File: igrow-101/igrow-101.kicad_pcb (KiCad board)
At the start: 2 copper layers, 49.8 x 39.5 mm, 30 parts, among them P1 CONN_02X05, Q1 NPN, Q2 NPN, Q3 NPN, SW1 SW_PUSH, U1 NRF51822-MODULE, U2 SHT21, U3 TL972

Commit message: Rework with 0.508mm/20mil minimum track widths
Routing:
- net GND: track 0.00 -> 115.4 mm
- net VCC: track 0.00 -> 88.7 mm, vias 0 -> 1
- net Net-(Q1-Pad2): track 0.00 -> 24.5 mm
- net Net-(Q2-Pad2): track 0.00 -> 17.6 mm
- net Net-(R10-Pad2): track 0.00 -> 13.8 mm
- net Net-(R3-Pad2): track 0.00 -> 13.2 mm
- net Net-(Q3-Pad2): track 0.00 -> 12.0 mm
- net Net-(R2-Pad2): track 0.00 -> 11.4 mm
- net Net-(D4-Pad1): track 0.00 -> 10.5 mm
- net Net-(R1-Pad2): track 0.00 -> 9.58 mm
- net Net-(D4-Pad2): track 0.00 -> 8.86 mm
- net Net-(P1-Pad4): track 0.00 -> 7.10 mm
- net Net-(D3-Pad2): track 0.00 -> 6.00 mm
- net Net-(U1-Pad36): track 0.00 -> 5.73 mm
- net Net-(U1-Pad35): track 0.00 -> 5.70 mm
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- added copper zone on F.Cu, net GND

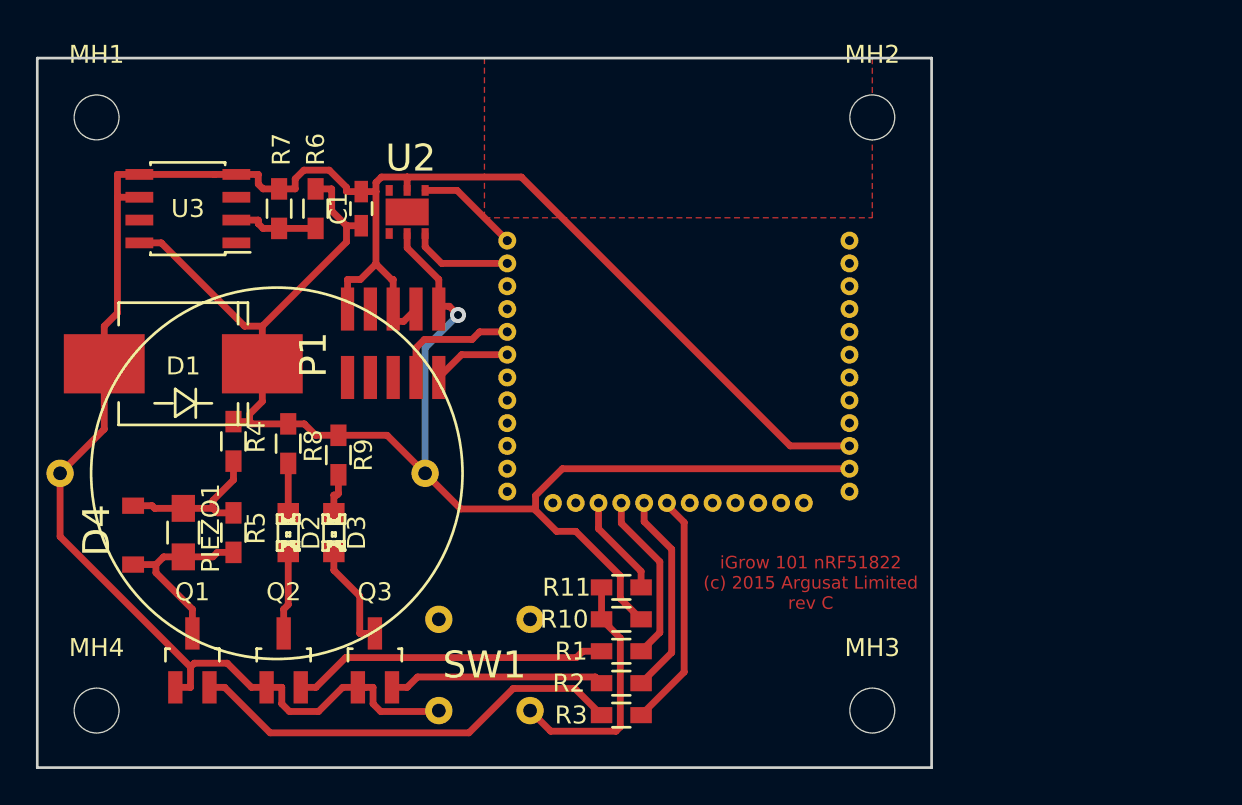
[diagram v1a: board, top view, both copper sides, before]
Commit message: First pass at board revision D - use direct connected IR LEDs for sensing
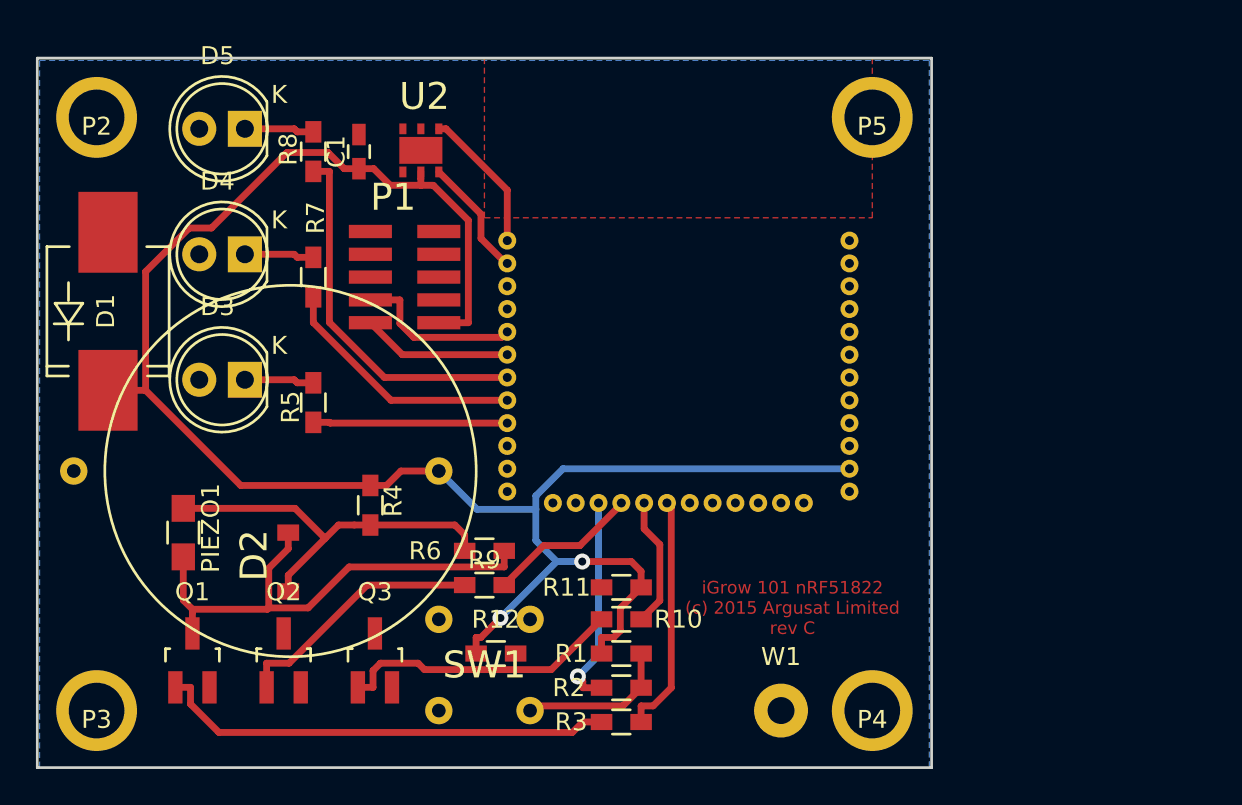
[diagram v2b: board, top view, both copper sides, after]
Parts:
- removed MH1, MH2, MH3, MH4: MountingHole_2-5mm, Mounting_Holes:MountingHole_2-5mm
- removed U3: TL972, Housings_SOIC:SOIC-8_3.9x4.9mm_Pitch1.27mm
- added D5: LED, LEDs:LED-5MM, F.Cu at (142.9, 97.2)
- added P2: CONN_01X01, igrow:MountingHole_M3, F.Cu at (134.6, 96.5)
- added P3: CONN_01X01, igrow:MountingHole_M3, F.Cu at (134.6, 129.5)
- added P4: CONN_01X01, igrow:MountingHole_M3, F.Cu at (177.8, 129.5)
- added P5: CONN_01X01, igrow:MountingHole_M3, F.Cu at (177.8, 96.5)
- added R12: R, Resistors_SMD:R_0603_HandSoldering, F.Cu at (156.8, 126.4)
- added W1: TEST_1P, Measurement_Points:Measurement_Point_Round-TH_Big, F.Cu at (172.7, 129.5)
- D2: value LED -> ZENER; footprint LEDs:LED-0805 -> igrow:SOD123
- D3: footprint LEDs:LED-0805 -> LEDs:LED-5MM
- D4: value ZENER -> LED; footprint igrow:SOD123 -> LEDs:LED-5MM
- Q1, Q2, Q3: footprint Housings_SOT-23_SOT-143_TSOT-6:SOT-23_Handsoldering -> igrow:SOT-23_Handsoldering_EBC
- moved R6 21.2 mm to (156.2, 120.7), turned to 0 degrees
- moved D4 18.4 mm to (142.9, 104.1), turned to 180 degrees
- moved R8 16.3 mm to (146.7, 98.4), turned to 90 degrees
- moved R9 10.9 mm to (156.2, 122.6), turned to 0 degrees
- moved D3 9.85 mm to (142.9, 111.1), turned to 180 degrees
- moved R5 8.49 mm to (146.7, 112.4), turned to 90 degrees
- moved R4 8.41 mm to (149.9, 118.1)
- moved D1 5.11 mm to (135.3, 107.3), turned to 270 degrees
- moved R7 4.26 mm to (146.7, 105.4)
- moved U2 3.51 mm to (153.7, 97.2)
- moved C1 3.18 mm to (149.2, 98.4)
- moved BT1 0.77 mm to (153.7, 116.2)
- moved P1 0.76 mm to (153.7, 108.0), turned to 180 degrees
- moved R3 0.38 mm to (163.8, 130.2)
- moved R2 0.25 mm to (163.8, 128.3)
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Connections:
- D3 pad 2: Net-(D3-Pad2) -> GND
- D4 pad 2: Net-(D4-Pad2) -> GND
- PIEZO1 pad 1: Net-(D4-Pad2) -> Net-(D2-Pad2)
- PIEZO1 pad 2: Net-(D4-Pad1) -> Net-(D2-Pad1)
- Q1 pad 3: Net-(D4-Pad1) -> Net-(D2-Pad1)
- Q2 pad 3: Net-(D2-Pad2) -> Net-(D6-Pad2)
- Q3 pad 3: Net-(D3-Pad2) -> Net-(D7-Pad2)
- R1 pad 1: Net-(Q2-Pad2) -> VCC
- R10 pad 1: VCC -> Net-(Q3-Pad2)
- R11 pad 1: Net-(R11-Pad1) -> VCC
- R11 pad 2: Net-(R10-Pad2) -> Net-(D6-Pad1)
- R2 pad 1: Net-(Q3-Pad2) -> Net-(R2-Pad1)
- R2 pad 2: Net-(R2-Pad2) -> Net-(R1-Pad2)
- R4 pad 2: Net-(D4-Pad2) -> Net-(D2-Pad2)
- R5 pad 1: Net-(D4-Pad2) -> Net-(R5-Pad1)
- R5 pad 2: Net-(D4-Pad1) -> Net-(D3-Pad1)
- R6 pad 1: VCC -> Net-(D2-Pad2)
- R6 pad 2: Net-(R6-Pad2) -> Net-(D2-Pad1)
- R7 pad 1: Net-(R6-Pad2) -> Net-(R7-Pad1)
- R7 pad 2: GND -> Net-(D4-Pad1)
- R8 pad 1: VCC -> Net-(R8-Pad1)
- R8 pad 2: Net-(D2-Pad1) -> Net-(D5-Pad1)
- R9 pad 1: VCC -> Net-(Q2-Pad2)
- R9 pad 2: Net-(D3-Pad1) -> Net-(R9-Pad2)
- SW1 pad 1: Net-(R10-Pad2) -> Net-(R1-Pad2)
- U1 pad 20: Net-(R2-Pad2) -> Net-(R10-Pad2)
- U1 pad 21: Net-(R1-Pad2) -> Net-(R9-Pad2)
- U1 pad 22: Net-(R11-Pad1) -> Net-(R2-Pad1)
- U1 pad 28: Net-(U1-Pad28) -> Net-(R5-Pad1)
- U1 pad 29: Net-(U1-Pad29) -> Net-(R7-Pad1)
- U1 pad 30: Net-(U1-Pad30) -> Net-(R8-Pad1)
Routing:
- net GND: track 115.4 -> 0.00 mm
- net Net-(D2-Pad1): track 2.80 -> 28.3 mm
- net Net-(R8-Pad1): track 0.00 -> 20.5 mm
- net Net-(D2-Pad2): track 4.67 -> 21.6 mm
- net VCC: track 88.7 -> 104.4 mm, vias 1 -> 2
- net Net-(R7-Pad1): track 0.00 -> 14.0 mm
- net Net-(R2-Pad1): track 0.00 -> 11.9 mm, vias 0 -> 1
- net Net-(R2-Pad2): track 11.4 -> 0.00 mm
- net Net-(R5-Pad1): track 0.00 -> 10.8 mm
- net Net-(D4-Pad2): track 8.86 -> 0.00 mm
- net Net-(R9-Pad2): track 0.00 -> 8.45 mm
- net Net-(D4-Pad1): track 10.5 -> 3.88 mm
- net Net-(R10-Pad2): track 13.8 -> 7.27 mm
- net Net-(D3-Pad2): track 6.00 -> 0.00 mm
- net Net-(R11-Pad1): track 5.68 -> 0.00 mm
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- added copper zone on B.Cu, net GND

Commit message: Revision D as sent to dirtypcbs for fab
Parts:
- added D6: LED, LEDs:LED_0805, B.Cu at (172.1, 123.2)
- added D7: LED, LEDs:LED_0805, B.Cu at (177.2, 123.2)
- BT1, D3, D4, D5: moved to B.Cu
- moved R12 24.2 mm to (179.1, 116.8), turned to 270 degrees
- moved Q2 15.6 mm to (160.0, 122.6)
- moved R6 14.5 mm to (142.9, 114.9)
- moved R3 12.1 mm to (151.8, 130.2)
- moved Q3 11.1 mm to (160.7, 130.2), turned to 270 degrees
- moved Q1 10.2 mm to (149.9, 124.5)
- moved BT1 5.12 mm to (153.0, 121.3), turned to 90 degrees
- moved R1 5.12 mm to (168.9, 127.0), turned to 270 degrees
- moved SW1 4.58 mm to (162.6, 127.0)
- moved R2 4.26 mm to (167.6, 130.2)
- moved R11 4.06 mm to (167.6, 121.3), turned to 0 degrees
- moved D3 3.17 mm to (142.9, 108.0)
- moved R9 3.17 mm to (154.3, 125.1), turned to 90 degrees
- moved D4 1.91 mm to (142.9, 102.2)
- moved R5 1.27 mm to (146.7, 111.1)
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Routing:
- net Net-(Q1-Pad2): track 25.6 -> 4.94 mm
- net Net-(D7-Pad2): track 0.00 -> 17.5 mm, vias 0 -> 1
- net Net-(D6-Pad2): track 0.00 -> 13.7 mm, vias 0 -> 1
- net Net-(Q2-Pad2): track 14.2 -> 5.65 mm
- net Net-(Q3-Pad2): track 16.0 -> 7.47 mm
- net Net-(R3-Pad2): track 13.4 -> 21.6 mm, vias 0 -> 1
- net Net-(D2-Pad1): track 28.3 -> 21.2 mm
- net Net-(R1-Pad2): track 8.61 -> 15.6 mm
- net Net-(R8-Pad1): track 20.5 -> 26.8 mm
- net Net-(R9-Pad2): track 8.45 -> 13.9 mm
- net Net-(D7-Pad1): track 0.00 -> 5.04 mm, vias 0 -> 1
- net Net-(D6-Pad1): track 0.00 -> 4.14 mm, vias 0 -> 1
- net Net-(P1-Pad4): track 9.38 -> 13.4 mm, vias 0 -> 1
- net VCC: track 104.4 -> 102.1 mm, vias 2 -> 0
- net Net-(R2-Pad1): track 11.9 -> 13.8 mm, vias 1 -> 0
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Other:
- board text added: "iGrow 101 (c) 2015 - 2016 Argusat Limited rev D"
- board text removed: "iGrow 101 nRF51822 (c) 2015 Argusat Limited rev C"
